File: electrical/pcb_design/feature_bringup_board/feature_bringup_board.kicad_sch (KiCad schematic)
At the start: 23 parts, among them J1 Sensor Signal, J10 Molex_504050-0691, J11 Button_Socket, J12 Button_Socket, J13 Button_Socket, J2 Sensor PWR, J3 External SPI, J4 External Power, J5 Power Selection, J6 STLINK, J9 Molex_504050-0691, U1 STM32L452RCT6, U2 BMI323, U3 BMI323

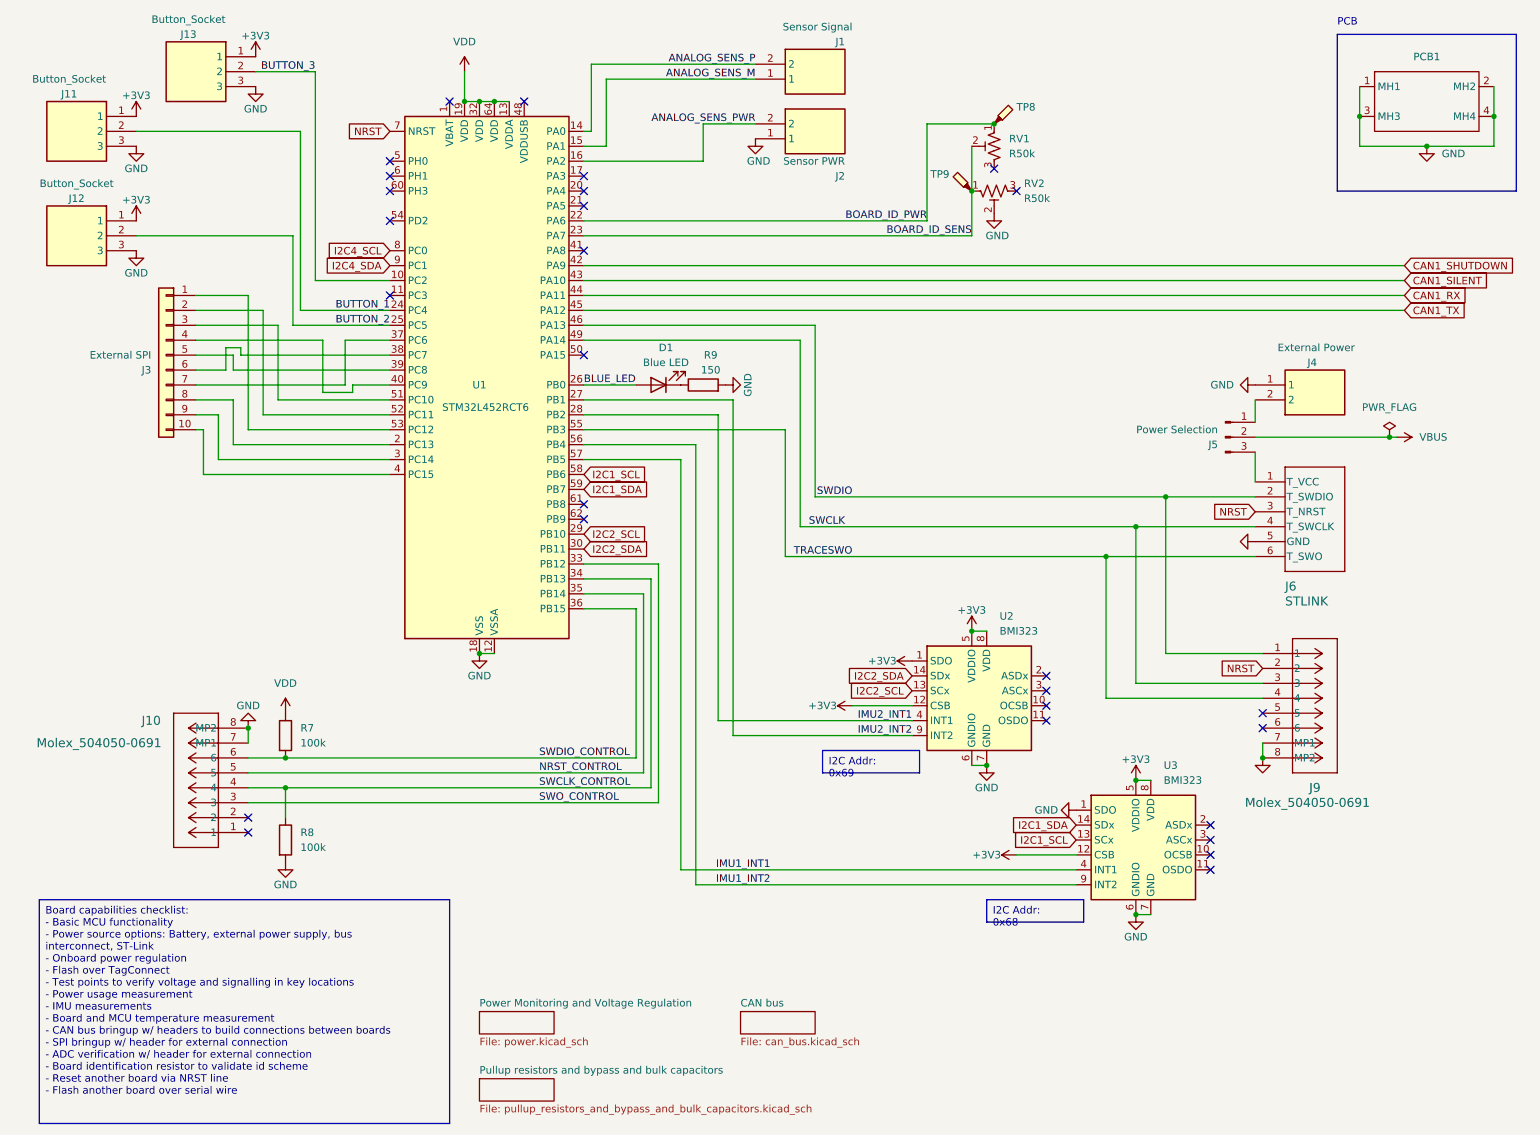
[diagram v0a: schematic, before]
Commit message: Added pull-up and pull-down resistors on NRST and BOOT0. Moved IMUs to separate sheet to improve readability.
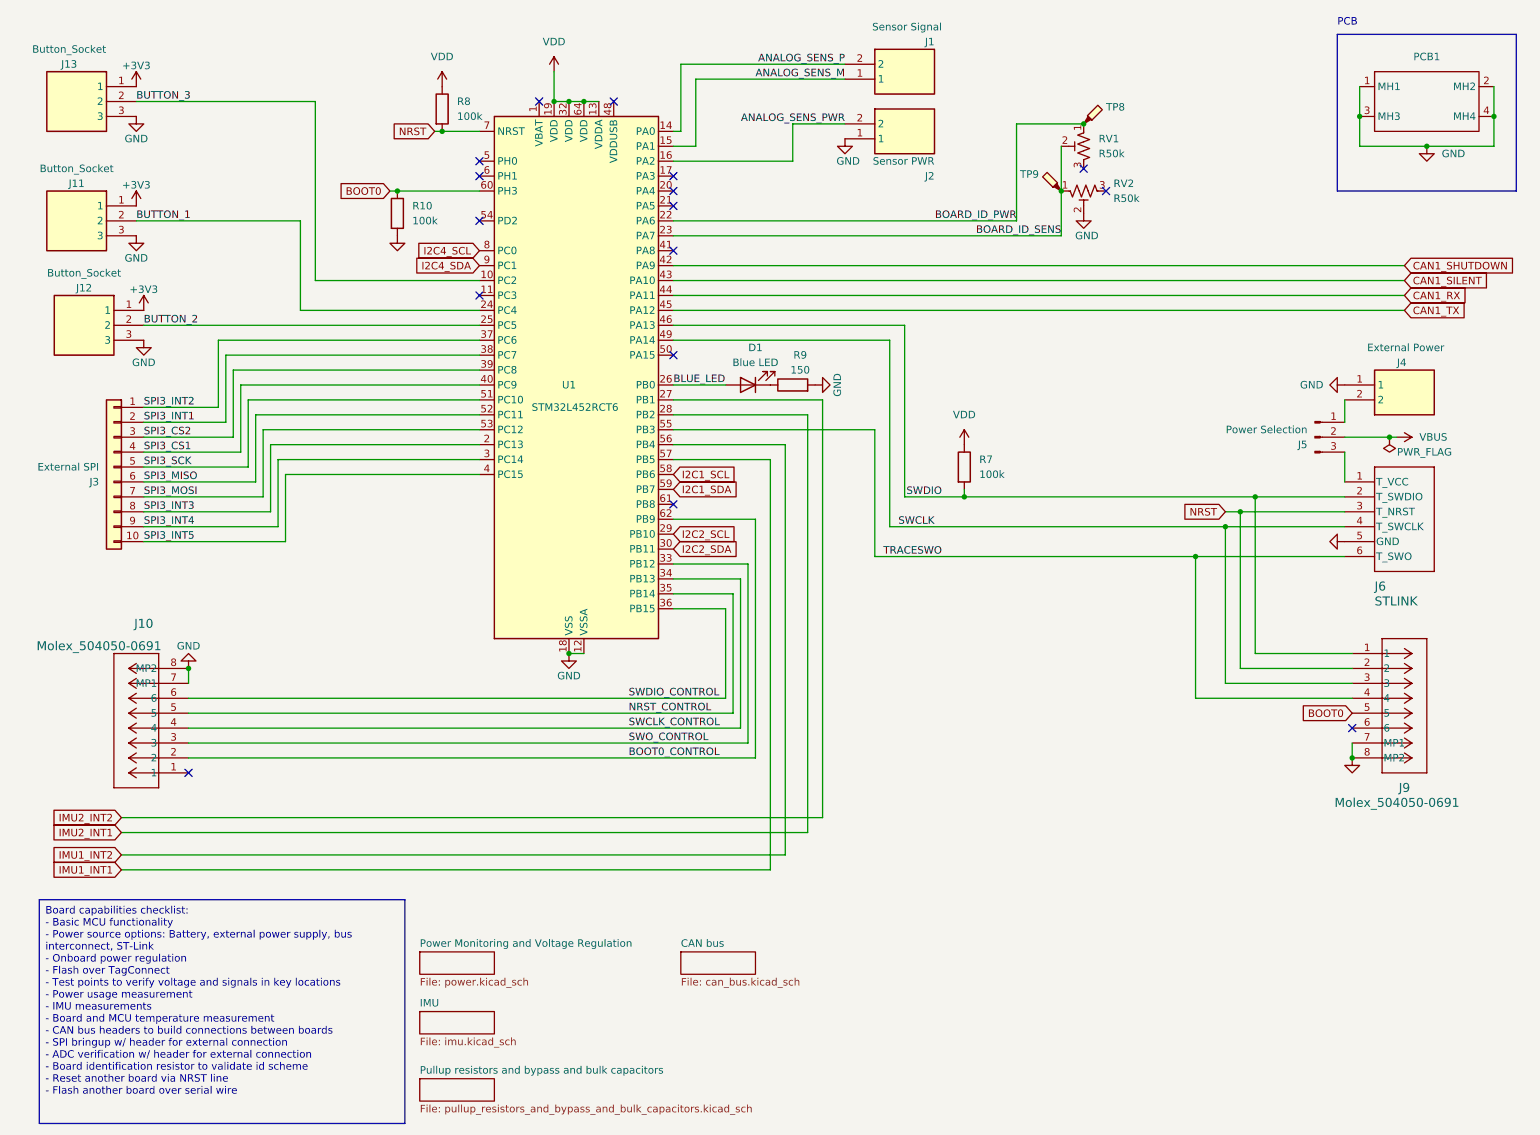
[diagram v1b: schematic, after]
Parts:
- removed U2, U3: BMI323, Package_LGA:Bosch_LGA-14_3x2.5mm_P0.5mm, symbol Sensor_Motion:BMI160
- added R10: 100k, footprints:Nondescript_R_0402_1005Metric, symbol Device:R
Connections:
- net GND: now also R10.2; no longer R8.2
- net NRST: now also R8.2
- net SWCLK_CONTROL: no longer R8.1
- net SWDIO: now also R7.2
- net SWDIO_CONTROL: no longer R7.2
- net VDD: now also R8.1
- net SPI3_INT3: now reaches J3.8 (Pin_8), U1.2 (PC13)
- net SPI3_INT4: now reaches J3.9 (Pin_9), U1.3 (PC14)
- net SPI3_INT2: now reaches U1.37 (PC6)
- net SPI3_INT2: now also J3.1 (Pin_1); no longer J3.7 (Pin_7)
- net SPI3_INT1: now reaches U1.38 (PC7)
- net SPI3_INT1: now also J3.2 (Pin_2); no longer J3.6 (Pin_6)
- net SPI3_CS2: now reaches U1.39 (PC8)
- net SPI3_CS2: now also J3.3 (Pin_3); no longer J3.5 (Pin_5)
- net SPI3_INT5: now reaches J3.10 (Pin_10), U1.4 (PC15)
- net SPI3_CS1: now reaches J3.4 (Pin_4), U1.40 (PC9)
- net SPI3_SCK: now reaches U1.51 (PC10)
- net SPI3_SCK: now also J3.5 (Pin_5); no longer J3.3 (Pin_3)
- net SPI3_MISO: now reaches U1.52 (PC11)
- net SPI3_MISO: now also J3.6 (Pin_6); no longer J3.2 (Pin_2)
- net SPI3_MOSI: now reaches U1.53 (PC12)
- net SPI3_MOSI: now also J3.7 (Pin_7); no longer J3.1 (Pin_1)
- net BOOT0: now reaches U1.60 (PH3)
- net BOOT0: now also J9.5, R10.1
- net BOOT0_CONTROL: now reaches U1.62 (PB9)
- net BOOT0_CONTROL: now also J10.2
- no-connect marks 28 -> 16
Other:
- added sheet IMU (imu.kicad_sch)
- moved on the sheet: D1, J1, J10, J11, J12, J13, J2, J4, J5, J6, J9, R9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

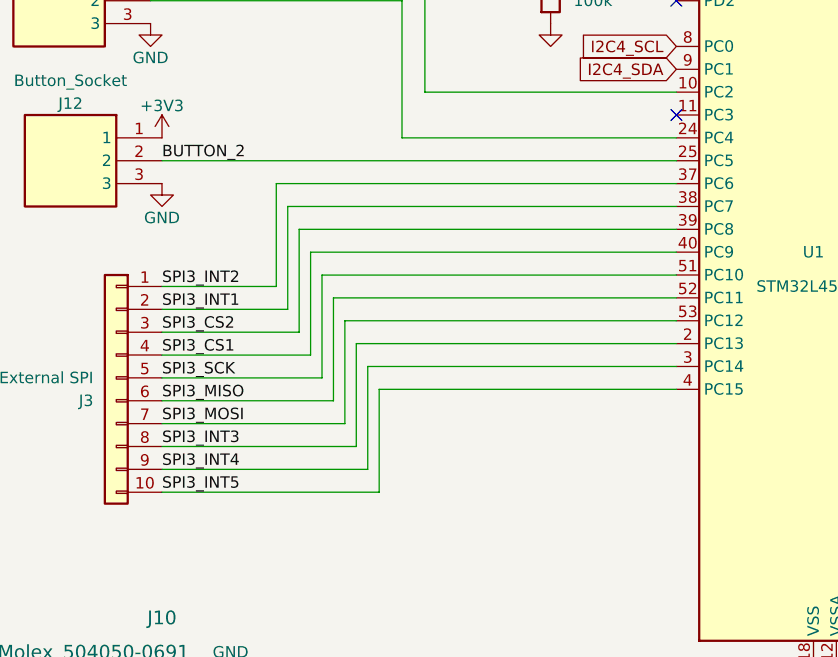
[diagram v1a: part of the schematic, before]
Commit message: Updated PCB layout to include pull-up and pull-down resistors on NRST and BOOT0.
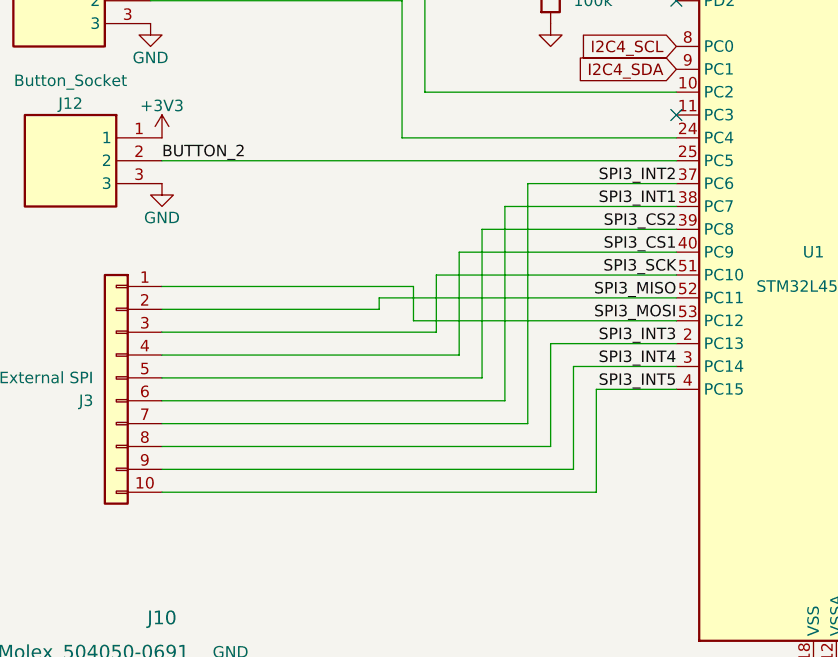
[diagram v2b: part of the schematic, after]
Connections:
- net SPI3_CS2: now also J3.5 (Pin_5); no longer J3.3 (Pin_3)
- net SPI3_INT1: now also J3.6 (Pin_6); no longer J3.2 (Pin_2)
- net SPI3_INT2: now also J3.7 (Pin_7); no longer J3.1 (Pin_1)
- net SPI3_MISO: now also J3.2 (Pin_2); no longer J3.6 (Pin_6)
- net SPI3_MOSI: now also J3.1 (Pin_1); no longer J3.7 (Pin_7)
- net SPI3_SCK: now also J3.3 (Pin_3); no longer J3.5 (Pin_5)

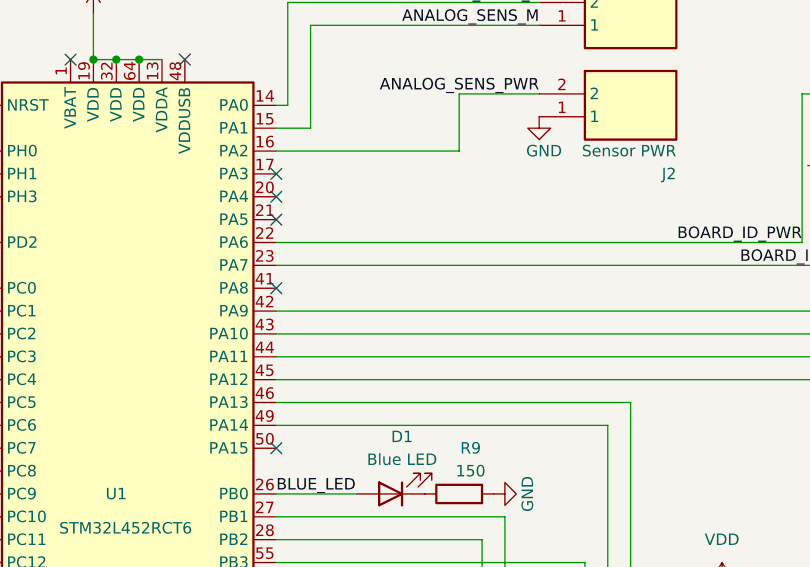
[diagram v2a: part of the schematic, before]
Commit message: Added a test point to monitor the master clock output (MCO). This should be configurable in software to allow us to monitor MSI, PLLCLK, LSI, HSI 48, and SYSCLK.
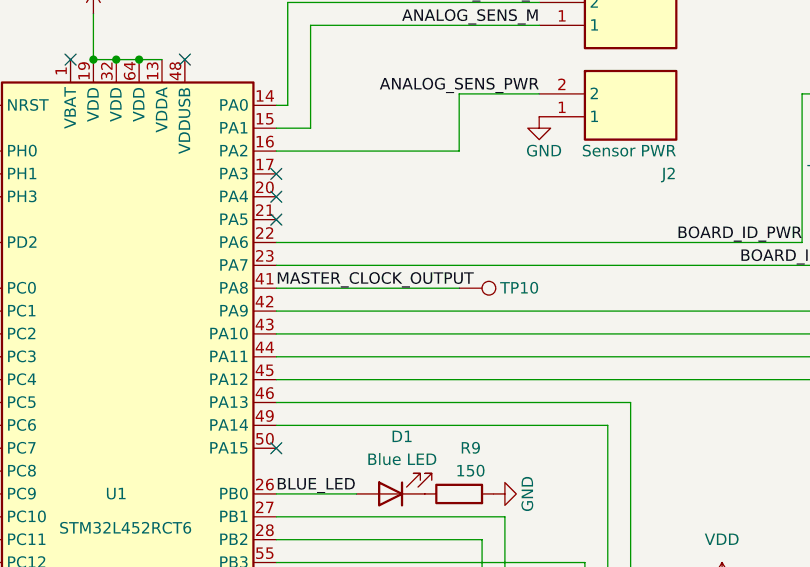
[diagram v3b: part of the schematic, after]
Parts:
- added TP10: TestPoint, footprints:Keystone_5001, symbol TVSC:TestPoint_Keystone_5002
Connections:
- net MASTER_CLOCK_OUTPUT: now reaches U1.41 (PA8)
- net MASTER_CLOCK_OUTPUT: now also TP10.1
- no-connect marks 16 -> 15
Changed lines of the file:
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@@
   (no_connect (at 121.92 71.12))
   (no_connect (at 99.06 27.94))
-  (no_connect (at 121.92 53.34))
   (no_connect (at 111.76 27.94))
   (no_connect (at 88.9 60.96))
@@
     (stroke (width 0) (type default))
   )
+  (wire (pts (xy 121.92 53.34) (xy 142.24 53.34))
+    (stroke (width 0) (type default))
+  )
   (wire (pts (xy 58.42 48.26) (xy 58.42 63.5))
     (stroke (width 0) (type default))
@@
   (label "SWCLK" (at 166.37 100.33 180) (fields_autoplaced)
     (effects (font (size 1.27 1.27)) (justify right bottom))
+  )
+  (label "MASTER_CLOCK_OUTPUT" (at 121.92 53.34 0) (fields_autoplaced)
+    (effects (font (size 1.27 1.27)) (justify left bottom))
   )
   (label "TRACESWO" (at 167.64 105.41 180) (fields_autoplaced)
@@
         )
       )
+    )
+  )
+  (symbol (lib_id "TVSC:TestPoint_Keystone_5002") (at 142.24 53.34 270) (unit 1)
+    (in_bom yes) (on_board yes) (dnp no)
+    (property "Reference" "TP10" (at 151.13 53.34 90)
+      (effects (font (size 1.27 1.27)) (justify right))
+    )
+    (property "Value" "TestPoint" (at 146.812 50.8 0)
+      (effects (font (size 1.27 1.27)) (justify right) hide)
+    )
+    (property "Footprint" "footprints:Keystone_5001" (at 142.24 58.42 0)
+      (effects (font (size 1.27 1.27)) hide)
+    )
+    (property "Datasheet" "https://www.keyelco.com/product.cfm/product_id/1310" (at 142.24 58.42 0)
+      (effects (font (size 1.27 1.27)) hide)
+    )
+    (property "Color" "White" (at 142.24 58.42 0)
+      (effects (font (size 1.27 1.27)) hide)
+    )
+    (property "Manufacturer" "Keystone" (at 142.24 53.34 0)
+      (effects (font (size 1.27 1.27)) hide)
+    )
+    (property "Manufacturer Part Number" "5001" (at 142.24 53.34 0)
+      (effects (font (size 1.27 1.27)) hide)
+    )
+    (property "MPN" "C238122" (at 142.24 53.34 0)
+      (effects (font (size 1.27 1.27)) hide)
+    )
+    (property "Active" "Y" (at 142.24 53.34 0)
+      (effects (font (size 1.27 1.27)) hide)
+    )
+    (pin "1")
+    (instances
+      (project "feature_bringup_board"
+        (path "/695f882b-5312-4493-b26d-8f7d6768a9db"
+          (reference "TP10") (unit 1)
+        )
+      )

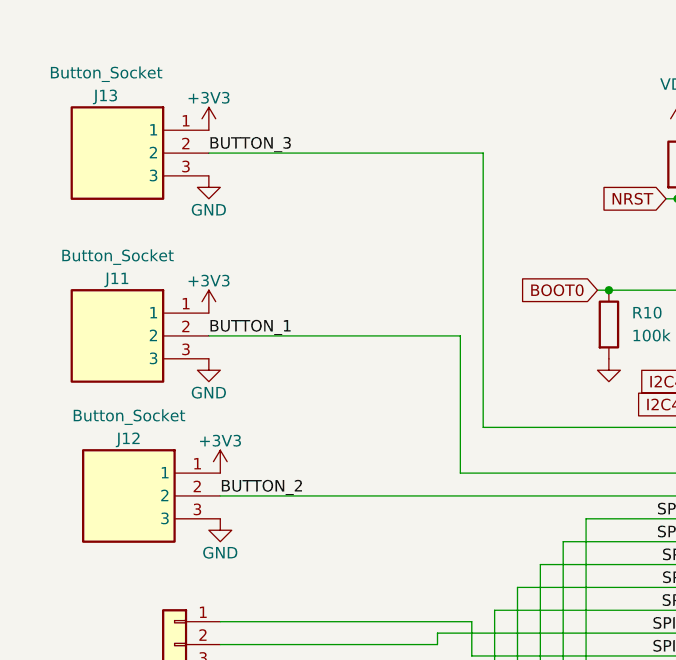
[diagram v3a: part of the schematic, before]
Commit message: Rename buttons to help remember which button is capable of waking the board from shutdown.
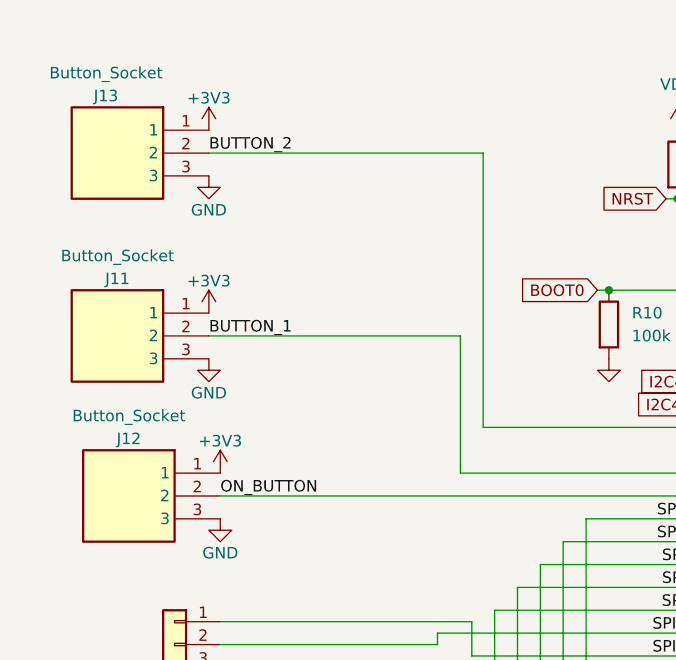
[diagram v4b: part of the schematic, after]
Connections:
- net BUTTON_3 is gone; now on net BUTTON_2: J13.2, U1.10 (PC2)
- net BUTTON_2: no longer J12.2, U1.25 (PC5)
- new net ON_BUTTON: J12.2, U1.25 (PC5)
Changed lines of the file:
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@@
     (effects (font (size 1.27 1.27)) (justify right bottom))
   )
-  (label "BUTTON_2" (at 31.75 66.04 0) (fields_autoplaced)
+  (label "ON_BUTTON" (at 31.75 66.04 0) (fields_autoplaced)
     (effects (font (size 1.27 1.27)) (justify left bottom))
   )
@@
     (effects (font (size 1.27 1.27)) (justify right bottom))
   )
-  (label "BUTTON_3" (at 30.48 27.94 0) (fields_autoplaced)
+  (label "BUTTON_2" (at 30.48 27.94 0) (fields_autoplaced)
     (effects (font (size 1.27 1.27)) (justify left bottom))
   )
